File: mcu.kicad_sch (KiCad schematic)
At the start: 42 parts, among them J2 RJ45_Shielded, J3 RJ45_Shielded, J4 Micro_SD_Card_Det1, J6 Conn_01x03_Pin, J7 Conn_01x05_Pin, SW1 SW_Push, SW2 SW_Push, SW3 SW_Push, SW4 SW_Push, U1 nRF52840-QIXX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

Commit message: add inductor and crystal
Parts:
- Y2: footprint (none) -> Library:CRYSTAL-SMD_L3.2-W1.5-1; Model (none) -> NDK NX3215SA-32.768K-STD-MUA-9
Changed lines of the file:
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@@
 			)
 		)
-		(property "Footprint" ""
+		(property "Footprint" "Library:CRYSTAL-SMD_L3.2-W1.5-1"
 			(at 73.66 96.52 0)
 			(effects
@@
 			(effects
 				(font
+					(size 1.27 1.27)
+				)
+				(hide yes)
+			)
+		)
+		(property "Model" "NDK NX3215SA-32.768K-STD-MUA-9 "
+			(at 73.66 96.52 90)
+			(effects
+				(font

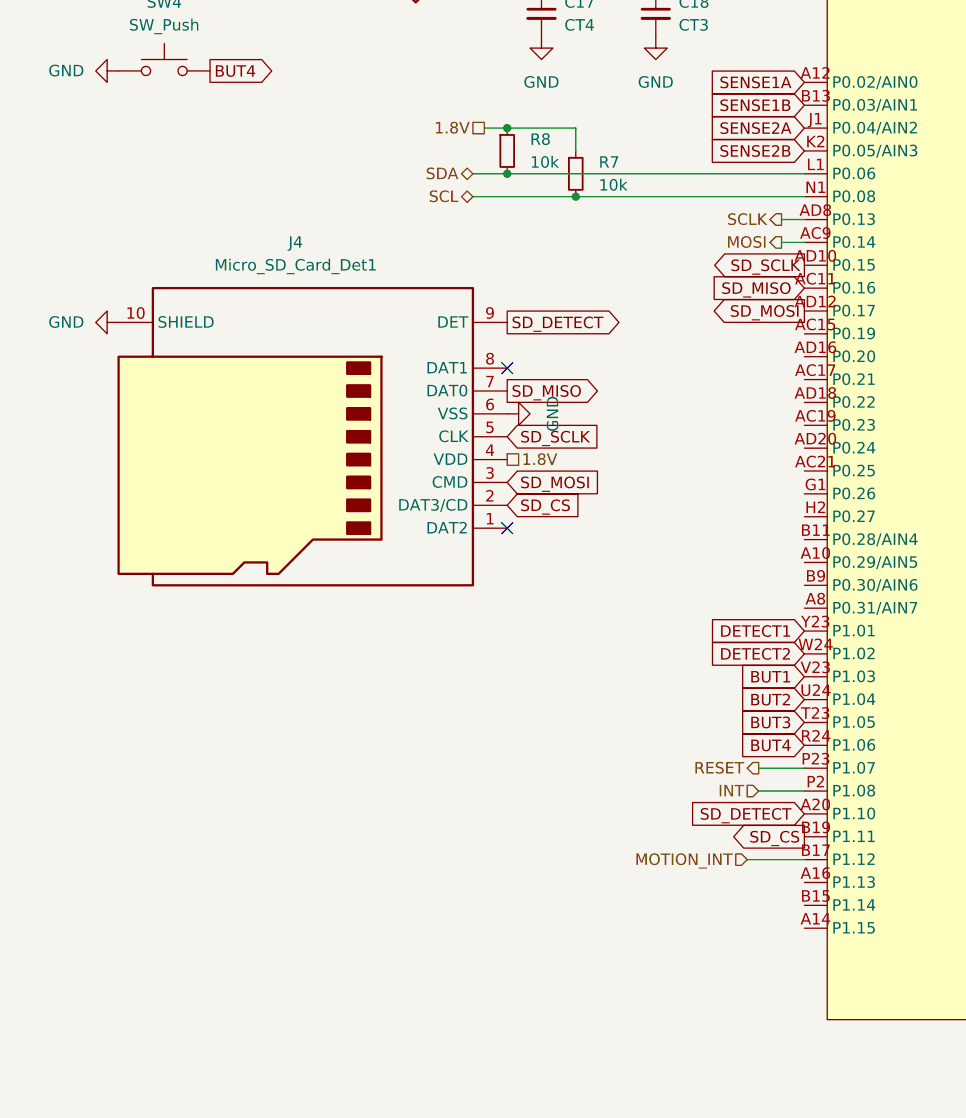
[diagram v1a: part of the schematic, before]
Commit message: use separate i2c bus for PMIC
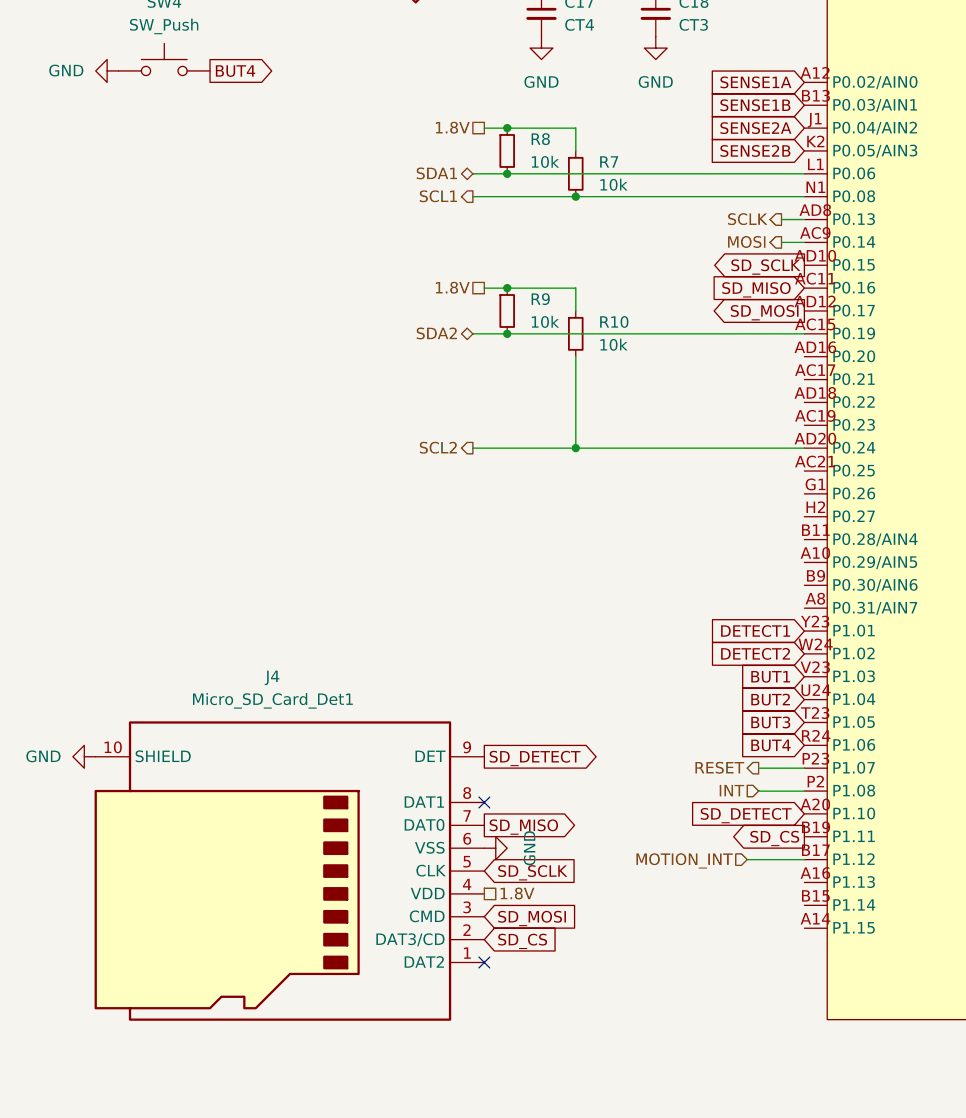
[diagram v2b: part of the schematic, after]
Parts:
- added R10, R9: 10k, Resistor_SMD:R_0402_1005Metric, symbol Device:R_Small
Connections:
- net 1.8V: now also R10.1, R9.1
- net SDA2: now reaches U1.AC15 (P0.19)
- net SDA2: now also R9.2
- net SCL2: now reaches U1.AD20 (P0.24)
- net SCL2: now also R10.2
- net SCL renamed SCL1
- net SDA renamed SDA1
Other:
- moved on the sheet: J4

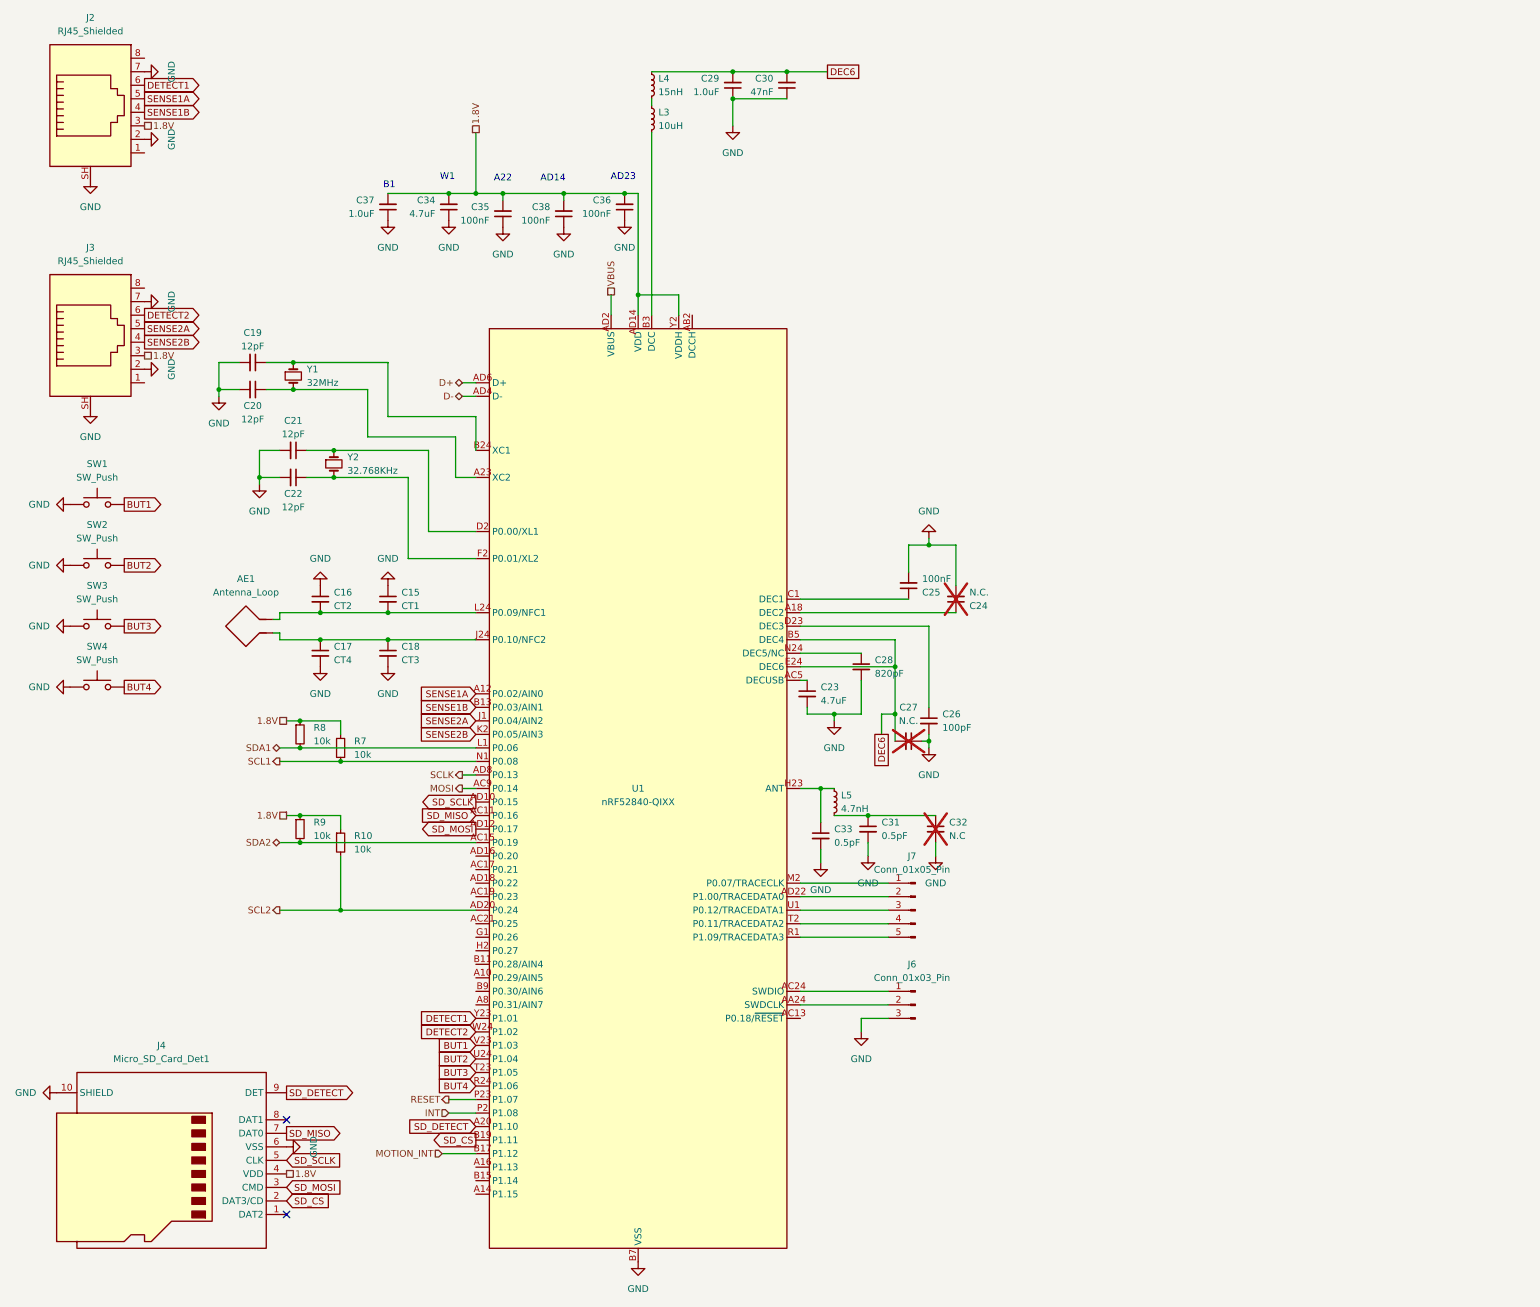
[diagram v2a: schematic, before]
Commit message: switch out SoC, stuff is in the air
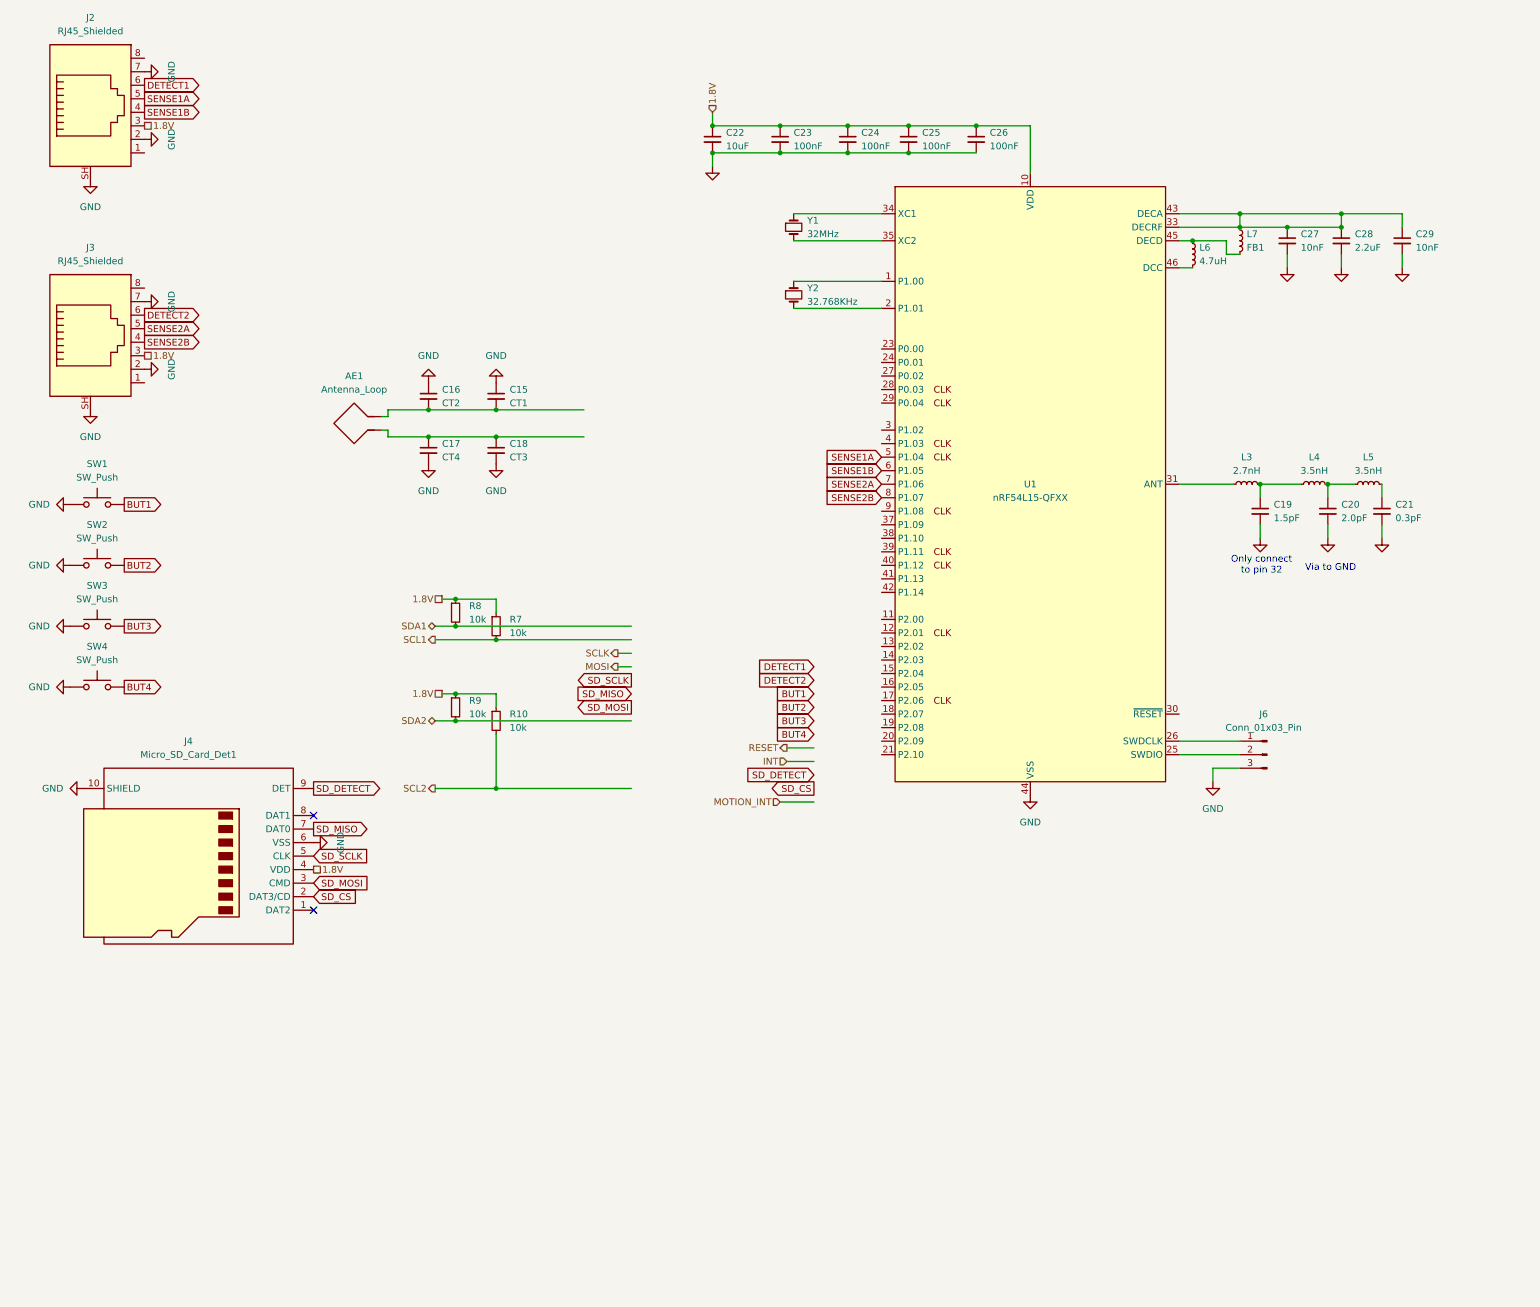
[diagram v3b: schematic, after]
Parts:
- removed C30: 47nF, Capacitor_SMD:C_0402_1005Metric, symbol Device:C_Small
- removed C31, C33: 0.5pF, Capacitor_SMD:C_0402_1005Metric, symbol Device:C_Small
- removed C32: N.C, symbol Device:C_Small
- removed C34: 4.7uF, Capacitor_SMD:C_0402_1005Metric, symbol Device:C_Small
- removed C35, C36, C38: 100nF, Capacitor_SMD:C_0402_1005Metric, symbol Device:C_Small
- removed C37: 1.0uF, Capacitor_SMD:C_0402_1005Metric, symbol Device:C_Small
- removed J7: Conn_01x05_Pin, Connector_PinHeader_1.00mm:PinHeader_1x05_P1.00mm_Vertical, symbol Connector:Conn_01x05_Pin
- removed U1: nRF52840-QIXX, Package_DFN_QFN:Nordic_AQFN-73-1EP_7x7mm_P0.5mm, symbol PCM_nordic-lib-kicad-nrf52:nRF52840-QIXX
- added L6: 4.7uH, symbol Device:L_Small
- added L7: FB1, symbol Device:L_Small
- added U1: nRF54L15-QFXX, Package_DFN_QFN:QFN-48-1EP_6x6mm_P0.4mm_EP4.6x4.6mm_ThermalVias, symbol PCM_nordic-lib-kicad-nrf54l:nRF54L15-QFXX
- C19: value 12pF -> 1.5pF; footprint Capacitor_SMD:C_0402_1005Metric -> (none)
- C20: value 12pF -> 2.0pF; footprint Capacitor_SMD:C_0402_1005Metric -> (none)
- C21: value 12pF -> 0.3pF; footprint Capacitor_SMD:C_0402_1005Metric -> (none)
- C22: value 12pF -> 10uF; footprint Capacitor_SMD:C_0402_1005Metric -> (none)
- C23: value 4.7uF -> 100nF; footprint Capacitor_SMD:C_0402_1005Metric -> (none)
- C24: value N.C. -> 100nF; now fitted
- C25: footprint Capacitor_SMD:C_0402_1005Metric -> (none)
- C26: value 100pF -> 100nF; footprint Capacitor_SMD:C_0402_1005Metric -> (none)
- C27: value N.C. -> 10nF; now fitted
- C28: value 820pF -> 2.2uF; footprint Capacitor_SMD:C_0402_1005Metric -> (none)
- C29: value 1.0uF -> 10nF; footprint Capacitor_SMD:C_0402_1005Metric -> (none)
- J6: footprint Connector_PinHeader_1.00mm:PinHeader_1x03_P1.00mm_Vertical -> Connector_PinHeader_1.27mm:PinHeader_1x03_P1.27mm_Vertical
- L3: value 10uH -> 2.7nH
- L4: value 15nH -> 3.5nH
- L5: value 4.7nH -> 3.5nH
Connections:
- net 1.8V: now also C22.1, C23.1, C24.1, C25.1, C26.1, U1.10 (VDD), U1.22 (VDD), U1.36 (VDD), U1.47 (VDD), U1.48 (VDD)
- net GND: now also C27.2, C29.2, U1.32 (VSS_PA), U1.44 (VSS), U1.49 (VSS); no longer C27.1, C29.1
- net SENSE1A: now also U1.5 (P1.04)
- net SENSE1B: now also U1.6 (P1.05)
- net SENSE2A: now also U1.7 (P1.06)
- net SENSE2B: now also U1.8 (P1.07)
- net at C19.1: now also L3.2, L4.1; no longer Y1.1
- net at C20.1: now also L4.2, L5.1; no longer Y1.2
- net at J6.2 (Pin_2): now also U1.25 (SWDIO)
- net at J6.1 (Pin_1): now also U1.26 (SWDCLK)
- net at C21.1: now also L5.2; no longer Y2.1
- net at Y2.2: now also U1.2 (P1.01); no longer C22.1
- net at C28.1: now also C27.1, C29.1, L7.1, U1.33 (DECRF), U1.43 (DECA)
- net at L3.1: now also U1.31 (ANT); no longer L4.2
- removed net DEC6: C27.2, C29.2, L4.1
- new net: U1.34 (XC1), Y1.1
- new net: U1.35 (XC2), Y1.2
- new net: U1.1 (P1.00), Y2.1
- new net: L6.1, L7.2, U1.45 (DECD)
- new net: L6.2, U1.46 (DCC)
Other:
- note added: "Only connect to pin 32"
- note added: "Via to GND"
- note removed: "A22"
- note removed: "AD14"
- note removed: "AD23"
- note removed: "B1"
- note removed: "W1"
- moved on the sheet: AE1, C15, C16, C17, C18, J4, J6, R10, R7, R8, R9, Y1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

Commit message: re-integrate all components + add BT antenna
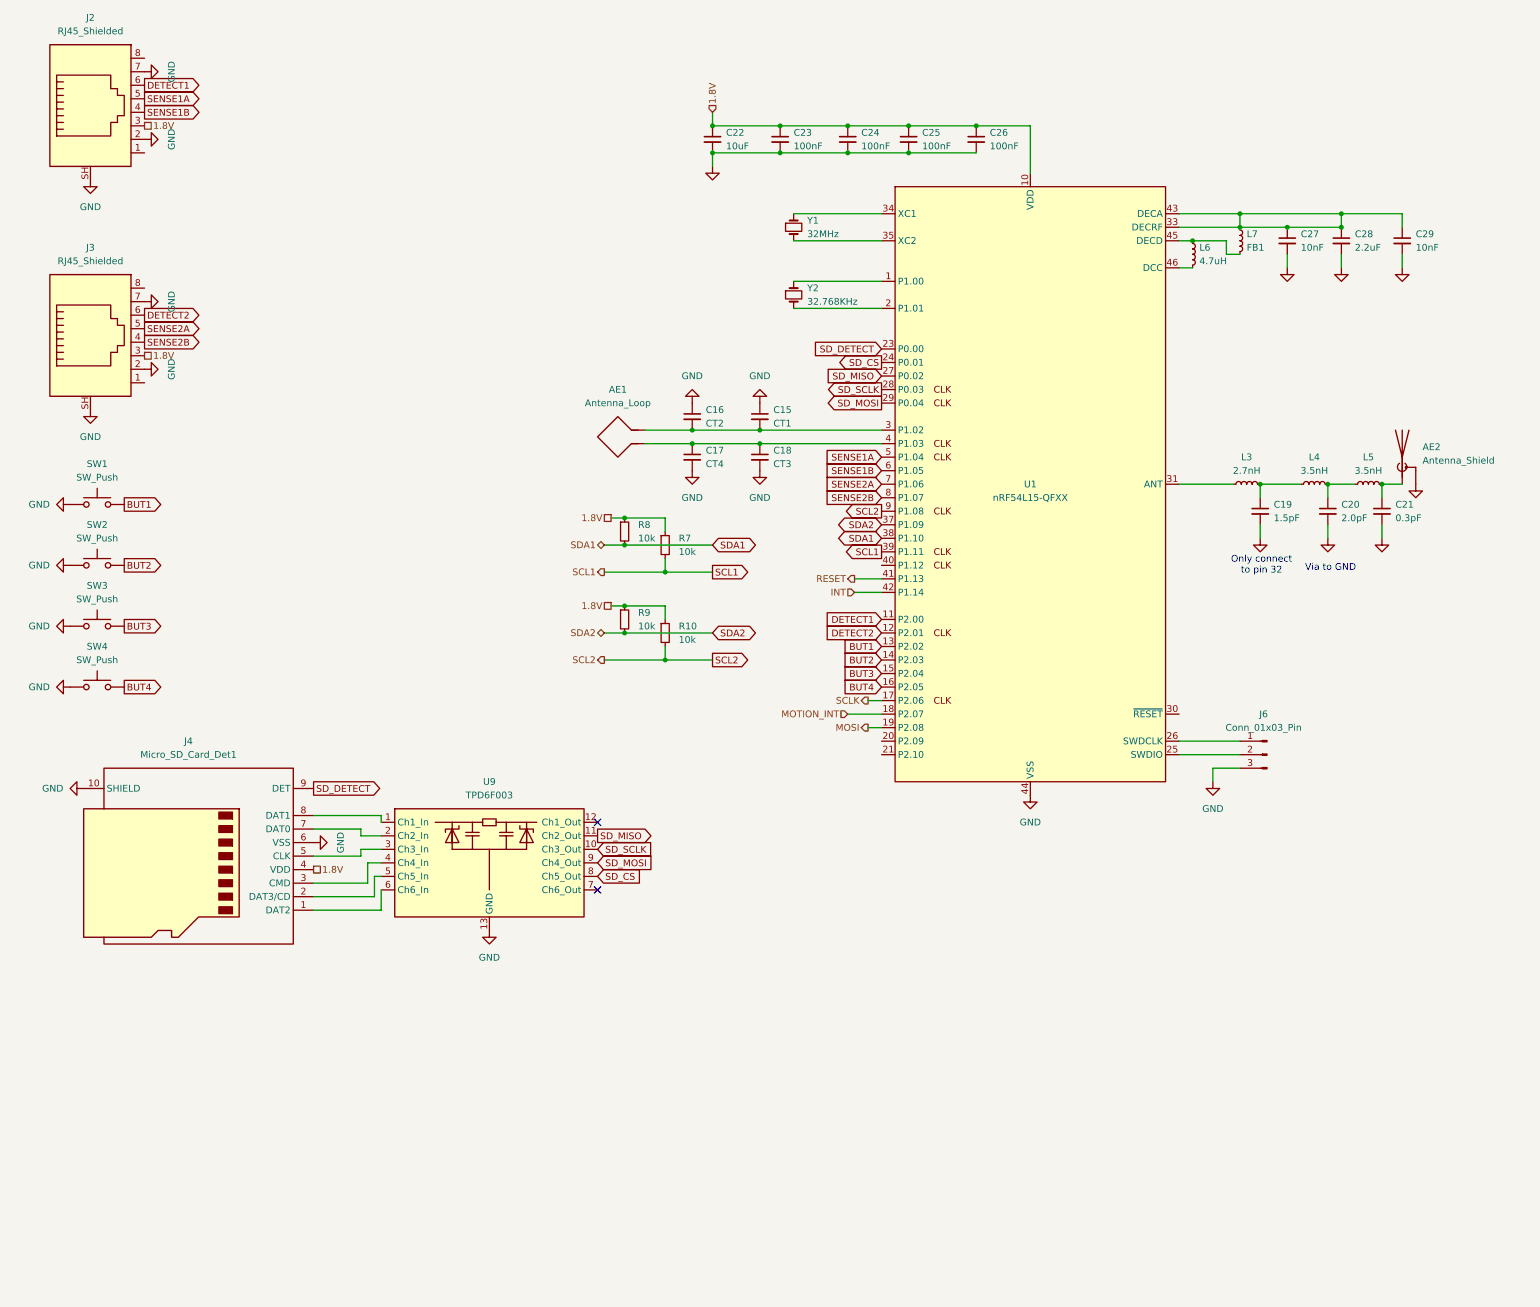
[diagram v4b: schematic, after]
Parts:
- added AE2: Antenna_Shield, RF_Antenna:Texas_SWRA117D_2.4GHz_Right, symbol Device:Antenna_Shield
- added U9: TPD6F003, Package_SON:Texas_R-PWSON-N12_EP0.4x2mm, symbol Power_Protection:TPD6F003
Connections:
- net BUT1: now also U1.13 (P2.02)
- net BUT2: now also U1.14 (P2.03)
- net BUT3: now also U1.15 (P2.04)
- net BUT4: now also U1.16 (P2.05)
- net DETECT1: now also U1.11 (P2.00)
- net DETECT2: now also U1.12 (P2.01)
- net GND: now also AE2.2 (Shield), U9.13 (GND)
- net INT: now also U1.42 (P1.14)
- net MOSI: now also U1.19 (P2.08)
- net MOTION_INT: now also U1.18 (P2.07)
- net RESET: now also U1.41 (P1.13)
- net SCL1: now also U1.39 (P1.11)
- net SCL2: now also U1.9 (P1.08)
- net SCLK: now also U1.17 (P2.06)
- net SDA1: now also U1.38 (P1.10)
- net SDA2: now also U1.37 (P1.09)
- net SD_CS: now also U1.24 (P0.01), U9.8 (Ch5_Out); no longer J4.2 (DAT3/CD)
- net SD_DETECT: now also U1.23 (P0.00)
- net SD_MISO: now also U1.27 (P0.02), U9.11 (Ch2_Out); no longer J4.7 (DAT0)
- net SD_MOSI: now also U1.29 (P0.04), U9.9 (Ch4_Out); no longer J4.3 (CMD)
- net SD_SCLK: now also U1.28 (P0.03), U9.10 (Ch3_Out); no longer J4.5 (CLK)
- net at C21.1, L5.2: now also AE2.1 (A)
- net at AE1.2, C15.2, C16.2: now also U1.3 (P1.02)
- net at U1.4 (P1.03): now also AE1.1, C17.1, C18.1
- net at J4.1 (DAT2): now also U9.6 (Ch6_In)
- net at J4.8 (DAT1): now also U9.1 (Ch1_In)
- new net: J4.7 (DAT0), U9.2 (Ch2_In)
- new net: J4.5 (CLK), U9.3 (Ch3_In)
- new net: J4.3 (CMD), U9.4 (Ch4_In)
- new net: J4.2 (DAT3/CD), U9.5 (Ch5_In)
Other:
- moved on the sheet: AE1, C15, C16, C17, C18, R10, R7, R8, R9
